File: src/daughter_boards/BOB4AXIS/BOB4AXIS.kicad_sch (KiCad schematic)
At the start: 43 parts, among them J1 Conn_02x13_Odd_Even, J1 Screw_Terminal_01x03, J2 Screw_Terminal_01x03, J3 Screw_Terminal_01x03, J4 Screw_Terminal_01x03, J5 Screw_Terminal_01x08, J6 Screw_Terminal_01x08, J7 Screw_Terminal_01x08, J8 Screw_Terminal_01x08, U1 LTV-814, U2 LTV-814, U3 LTV-814, U4 LTV-814, U5 AM26LS31CD, U6 AM26LS31CD, U7 KF142V-5_08-2P, U8 74HC86, U9 AM26LS31CD

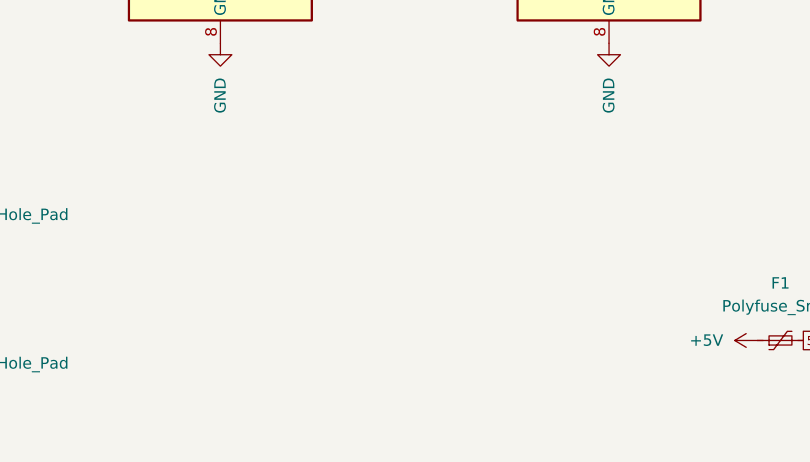
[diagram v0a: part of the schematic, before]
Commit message: Decoupling capacitors
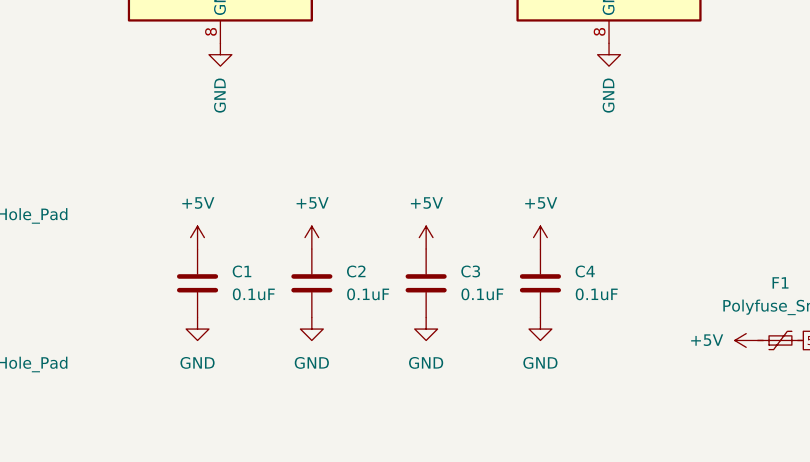
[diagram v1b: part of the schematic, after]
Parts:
- added C1, C2, C3, C4: 0.1uF, Capacitor_SMD:C_1206_3216Metric_Pad1.33x1.80mm_HandSolder, symbol Device:C
- F1: footprint Resistor_SMD:R_1210_3225Metric_Pad1.30x2.65mm_HandSolder -> Resistor_SMD:R_1812_4532Metric_Pad1.30x3.40mm_HandSolder
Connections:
- net +5V: now also C1.1, C2.1, C3.1, C4.1
- net GND: now also C1.2, C2.2, C3.2, C4.2
